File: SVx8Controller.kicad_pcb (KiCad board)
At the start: 2 copper layers, 85 x 120 mm, 59 parts, among them J1 Output, J2 Output, J3 Output, J4 Conn_01x10, J5 Conn_01x30, U1 MCP23017_SP, U2 MCP23017_SP

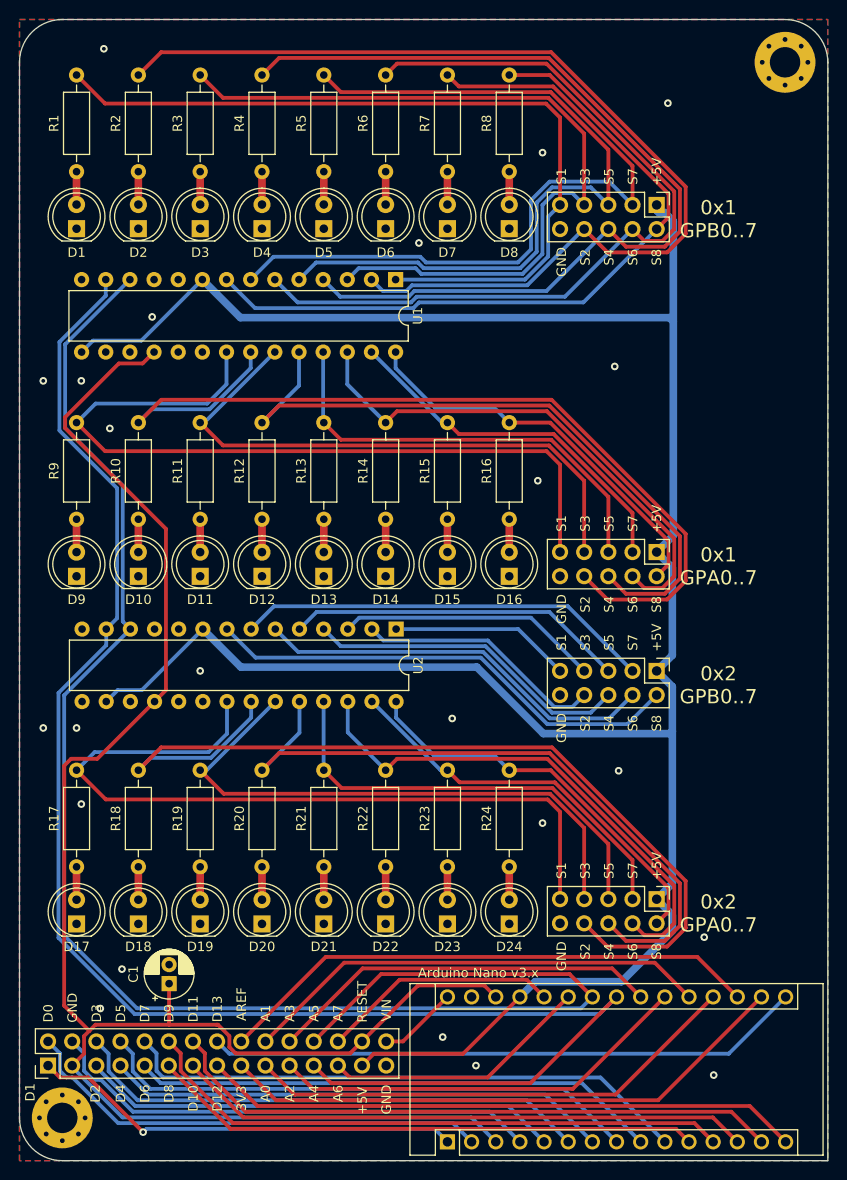
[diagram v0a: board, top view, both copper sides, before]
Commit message: Fix pin header
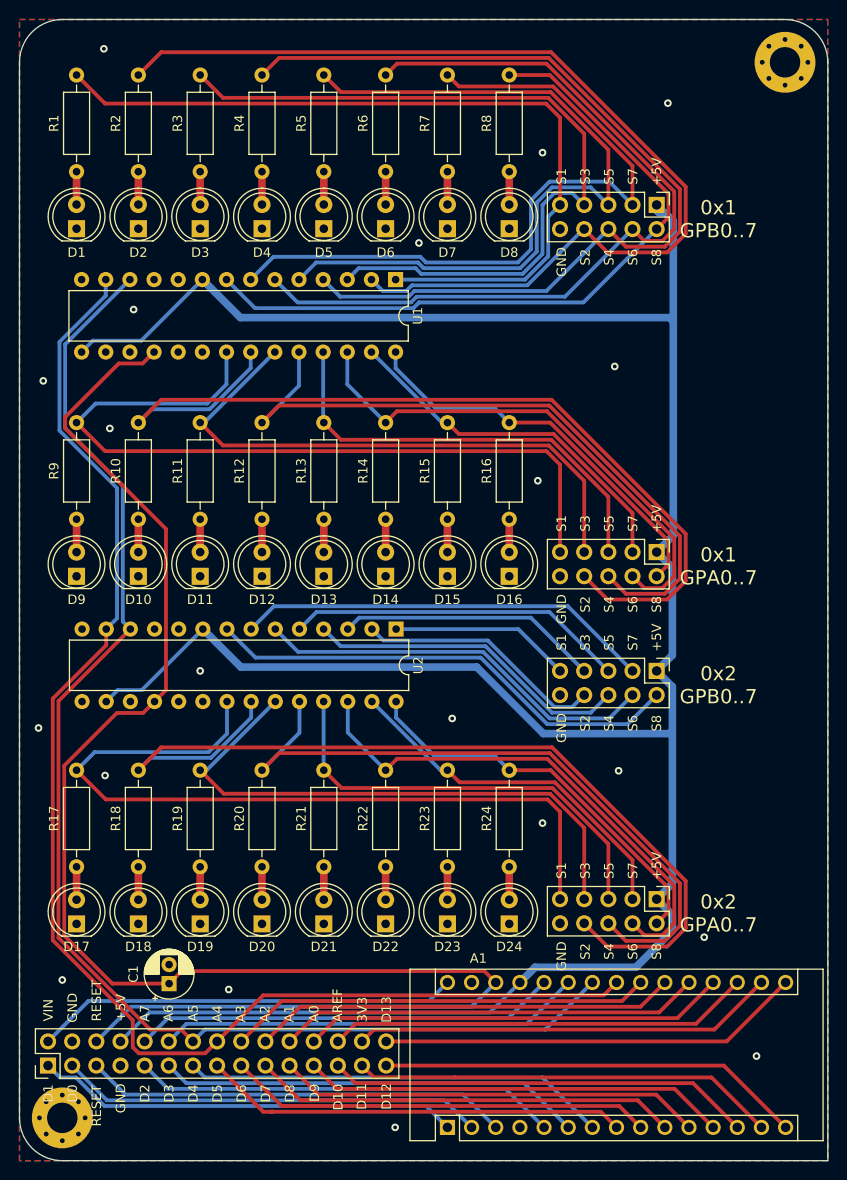
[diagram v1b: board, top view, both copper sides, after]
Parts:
- removed Arduino Nano v3.x: Arduino_Nano_v3.x, Module:Arduino_Nano
- added A1: Arduino_Nano_v3.x, Module:Arduino_Nano, F.Cu at (91.5, 142.5)
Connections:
- J5 pad 10: D7 -> A7
- J5 pad 11: D8 -> D3
- J5 pad 12: D9 -> A6
- J5 pad 13: D10 -> D4
- J5 pad 14: D11 -> A5
- J5 pad 15: D12 -> D5
- J5 pad 16: D13 -> A4
- J5 pad 17: 3V3 -> D6
- J5 pad 18: AREF -> A3
- J5 pad 19: A0 -> D7
- J5 pad 2: D0 -> VIN
- J5 pad 20: A1 -> A2
- J5 pad 21: A2 -> D8
- J5 pad 22: A3 -> A1
- J5 pad 23: A4 -> D9
- J5 pad 24: A5 -> A0
- J5 pad 25: A6 -> D10
- J5 pad 26: A7 -> AREF
- J5 pad 27: 5V -> D11
- J5 pad 28: RESET -> 3V3
- J5 pad 29: GND -> D12
- J5 pad 3: RESET -> D0
- J5 pad 30: VIN -> D13
- J5 pad 5: D2 -> RESET2
- J5 pad 6: D3 -> RESET
- J5 pad 7: D4 -> GND
- J5 pad 8: D5 -> 5V
- J5 pad 9: D6 -> D2
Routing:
- net GND: track 52.5 -> 0.00 mm, vias 23 -> 20
- net RESET2: track 0.00 -> 44.7 mm
- net VIN: track 8.38 -> 44.6 mm
- net A4: track 175.4 -> 145.7 mm
- net A5: track 170.0 -> 141.2 mm
- net 5V: track 254.6 -> 278.9 mm
- net RESET: track 193.9 -> 170.2 mm
- net D11: track 65.2 -> 44.7 mm
- net A7: track 25.1 -> 44.6 mm
- net D12: track 63.1 -> 44.7 mm
- net D13: track 62.8 -> 44.6 mm
- net D9: track 62.7 -> 44.7 mm
- net A6: track 28.2 -> 44.6 mm
- net 3V3: track 60.7 -> 44.6 mm
- net D10: track 60.7 -> 44.7 mm
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
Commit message: Add pull-up resistors
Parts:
- added R25: 10K, Resistor_THT:R_Axial_DIN0207_L6.3mm_D2.5mm_P10.16mm_Horizontal, F.Cu at (91.5, 59.5)
- added R26: 10K, Resistor_THT:R_Axial_DIN0207_L6.3mm_D2.5mm_P10.16mm_Horizontal, F.Cu at (91.5, 63.5)
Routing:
- net A4: track 145.7 -> 185.9 mm
- net A5: track 141.2 -> 177.2 mm
- net 5V: track 278.9 -> 285.2 mm
